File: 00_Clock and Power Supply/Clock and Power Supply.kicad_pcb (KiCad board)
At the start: 2 copper layers, 100 x 100 mm, 38 parts, among them J1 Output 1, J2 Output 2, J3 Jack-DC, Q1 TIP126, SW1 SPST, SW2 SPST, SW3 SW_SPDT, U1 L7805, U2 LM555xN, U3 LM555xN, U4 74LS01, U5 74LS01, U6 74LS01

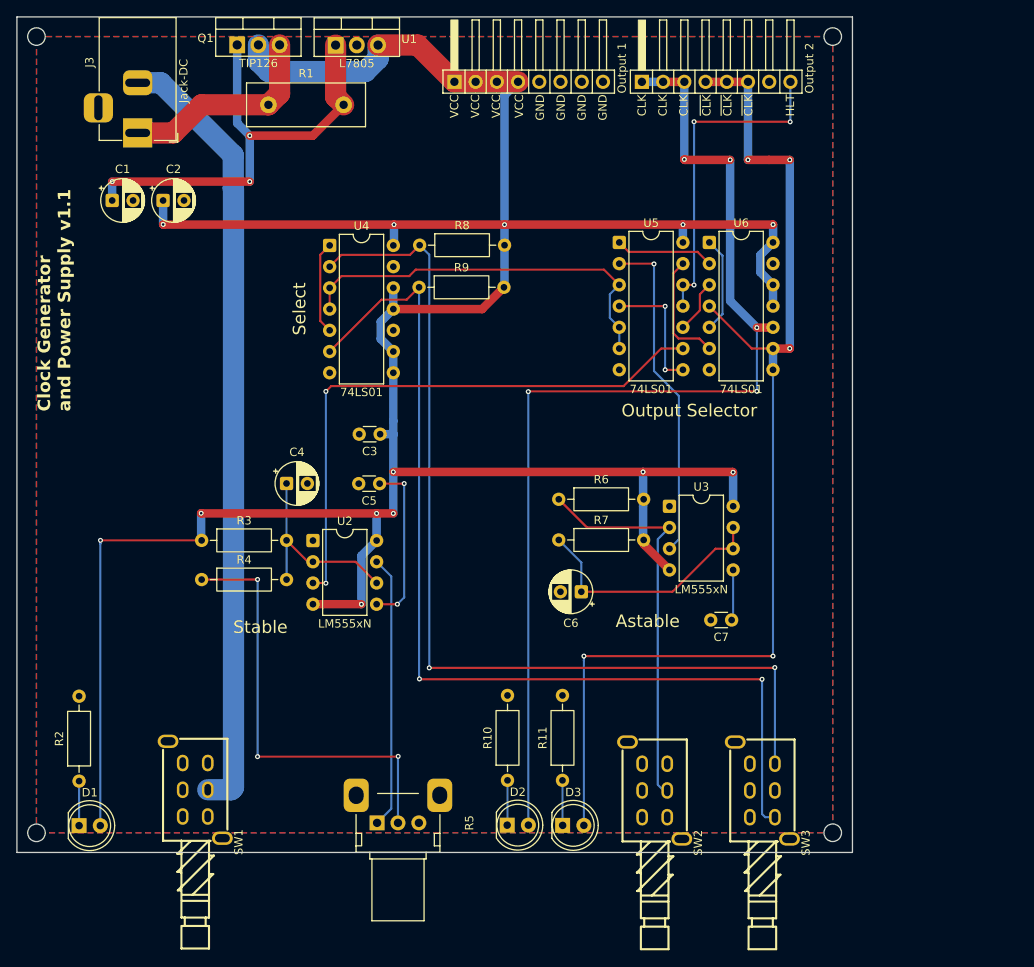
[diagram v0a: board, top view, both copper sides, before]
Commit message: Last revision of the cpu, all boards have been ordered. Implementation to be tested and documented in following commits.
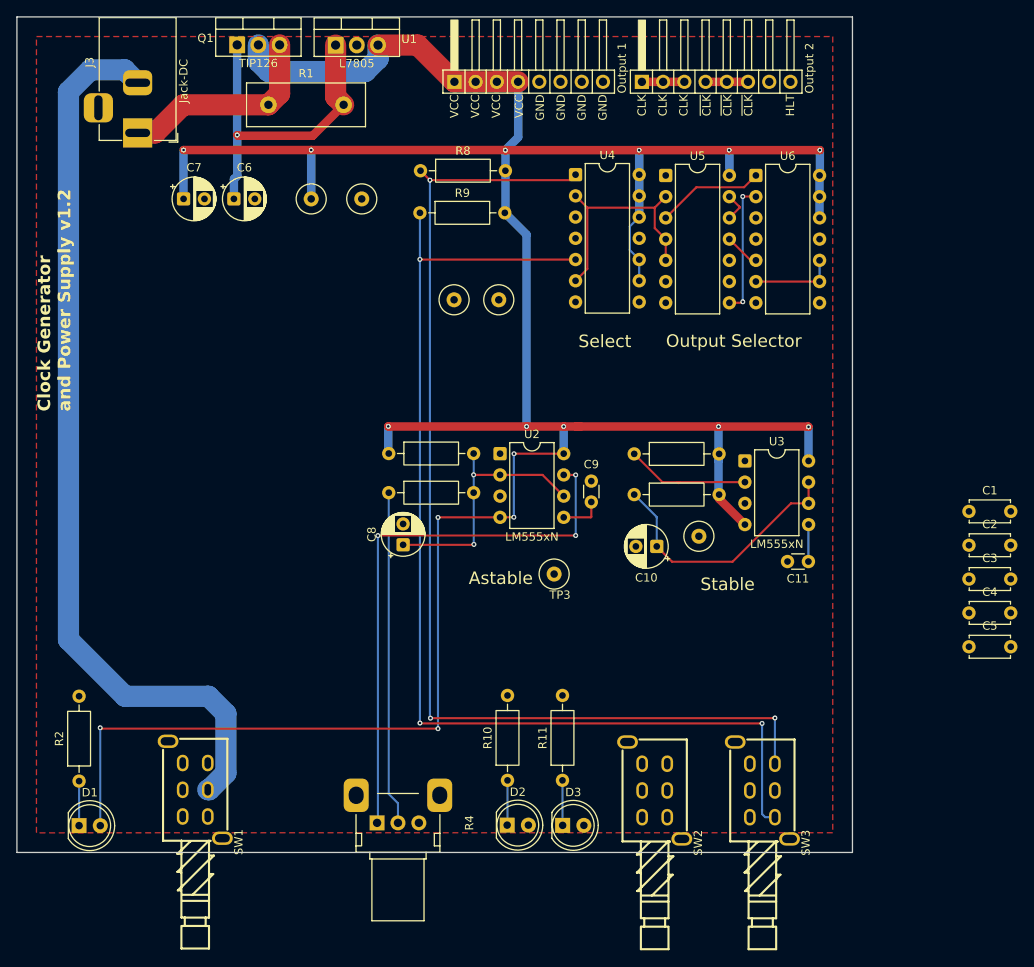
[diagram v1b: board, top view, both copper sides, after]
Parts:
- removed REF** (x4): MountingHole_2.1mm, MountingHole:MountingHole_2.1mm
- added C1: 100nF, Capacitor_THT:C_Disc_D4.7mm_W2.5mm_P5.00mm, F.Cu at (143.9, 89.2)
- added C2: 100nF, Capacitor_THT:C_Disc_D4.7mm_W2.5mm_P5.00mm, F.Cu at (143.9, 93.2)
- added C4: 100nF, Capacitor_THT:C_Disc_D4.7mm_W2.5mm_P5.00mm, F.Cu at (143.9, 101.3)
- added C5: 100nF, Capacitor_THT:C_Disc_D4.7mm_W2.5mm_P5.00mm, F.Cu at (143.9, 105.4)
- added TP1: VCC, TestPoint:TestPoint_Loop_D3.50mm_Drill0.9mm_Beaded, F.Cu at (65.2, 51.8)
- added TP2: GND, TestPoint:TestPoint_Loop_D3.50mm_Drill0.9mm_Beaded, F.Cu at (71.2, 51.8)
- added TP3: Astable, TestPoint:TestPoint_Loop_D3.50mm_Drill0.9mm_Beaded, F.Cu at (94.2, 96.7)
- added TP4: Stable, TestPoint:TestPoint_Loop_D3.50mm_Drill0.9mm_Beaded, F.Cu at (111.5, 92.2)
- added TP5: Select, TestPoint:TestPoint_Loop_D3.50mm_Drill0.9mm_Beaded, F.Cu at (82.2, 63.9)
- added TP6: HLT, TestPoint:TestPoint_Loop_D3.50mm_Drill0.9mm_Beaded, F.Cu at (87.6, 63.9)
- C3: value 100n -> 100nF; footprint Capacitor_THT:C_Disc_D3.0mm_W1.6mm_P2.50mm -> Capacitor_THT:C_Disc_D4.7mm_W2.5mm_P5.00mm
- U4, U5, U6: value 74LS01 -> 74LS00
- moved C3 72.6 mm to (143.9, 97.3), turned to 0 degrees
- moved U4 30.6 mm to (96.8, 48.9)
- moved C9 25.4 mm to (98.7, 88.1), turned to 90 degrees
- moved R3 24.7 mm to (74.4, 82.3)
- moved R5 24.7 mm to (74.4, 87.0)
- moved U2 24.7 mm to (87.8, 82.3)
- moved C8 15.8 mm to (76.2, 93.2), turned to 90 degrees
- moved C6 14.6 mm to (55.9, 51.8)
- moved C11 11.5 mm to (124.7, 95.2)
- moved R6 10.5 mm to (103.8, 82.3)
- moved R7 10.5 mm to (103.8, 87.2)
- moved U3 10.5 mm to (117.1, 83.2)
- moved C10 10.5 mm to (106.5, 93.4)
- moved U6 9.76 mm to (118.4, 49.0)
- moved U5 9.76 mm to (107.6, 49.0)
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- renumbered C6 to C10, C7 to C11, C1 to C6, C2 to C7, C4 to C8, C5 to C9, R5 to R4, R4 to R5
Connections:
- C3 pad 1: /VCC -> VCC
- C7 pad 1: /VCC -> VCC
- D1 pad 2: /VCC -> VCC
- D2 pad 2: /CLK -> CLK
- D3 pad 2: /~{CLK} -> ~{CLK}
- J1 pad 1: /VCC -> VCC
- J1 pad 2: /VCC -> VCC
- J1 pad 3: /VCC -> VCC
- J1 pad 4: /VCC -> VCC
- J2 pad 1: /CLK -> CLK
- J2 pad 2: /CLK -> CLK
- J2 pad 3: /CLK -> CLK
- J2 pad 4: /~{CLK} -> ~{CLK}
- J2 pad 5: /~{CLK} -> ~{CLK}
- J2 pad 6: /~{CLK} -> ~{CLK}
- J2 pad 8: /HLT -> HLT
- Q1 pad 2: /VCC -> VCC
- R3 pad 1: /VCC -> Net-(U2-DIS)
- R3 pad 2: Net-(U2-THR) -> VCC
- R4 pad 2: Net-(R4-Pad1) -> Net-(R4-Pad2)
- R5 pad 1: Net-(R4-Pad1) -> Net-(U2-THR)
- R5 pad 2: Net-(U2-THR) -> Net-(R4-Pad2)
- R6 pad 2: /VCC -> VCC
- R7 pad 2: /VCC -> VCC
- R8 pad 2: /VCC -> VCC
- R9 pad 2: /VCC -> VCC
- U1 pad 3: /VCC -> VCC
- U2 pad 4: /VCC -> VCC
- U2 pad 8: /VCC -> VCC
- U3 pad 4: /VCC -> VCC
- U3 pad 8: /VCC -> VCC
- U4 pad 1: Net-(U4-Pad1) -> Net-(SW3-A)
- U4 pad 10: unconnected-(U4-Pad10) -> VCC
- U4 pad 11: /VCC -> unconnected-(U4-Pad11)
- U4 pad 12: /VCC -> VCC
- U4 pad 13: unconnected-(U4-Pad13) -> VCC
- U4 pad 14: /VCC -> VCC
- U4 pad 2: Net-(SW3-A) -> /Clock Selector/Select
- U4 pad 3: /Clock Selector/Select -> Net-(U4-Pad3)
- U4 pad 4: /Clock Selector/Select -> Net-(U4-Pad3)
- U4 pad 5: Net-(U4-Pad1) -> Net-(SW3-C)
- U4 pad 6: Net-(SW3-C) -> /Clock Selector/Select
- U4 pad 8: /VCC -> unconnected-(U4-Pad8)
- U4 pad 9: /VCC -> VCC
- U5 pad 1: Net-(U5-Pad1) -> /Clock Selector/Stable
- U5 pad 10: Net-(U5-Pad10) -> /Astable Clock/Astable
- U5 pad 11: /HLT -> Net-(U5-Pad11)
- U5 pad 12: /HLT -> HLT
- U5 pad 13: Net-(U5-Pad13) -> HLT
- U5 pad 14: /VCC -> VCC
- U5 pad 2: /Clock Selector/Stable -> /Clock Selector/Select
- U5 pad 3: /Clock Selector/Select -> Net-(U5-Pad3)
- U5 pad 4: Net-(U5-Pad4) -> /Clock Selector/Select
- U5 pad 6: /Clock Selector/Select -> Net-(U5-Pad6)
- U5 pad 8: Net-(U5-Pad4) -> Net-(U5-Pad8)
- U5 pad 9: /Astable Clock/Astable -> Net-(U5-Pad6)
- U6 pad 1: Net-(U6-Pad1) -> Net-(U5-Pad3)
- U6 pad 10: /CLK -> ~{CLK}
- U6 pad 11: /VCC -> unconnected-(U6-Pad11)
- U6 pad 12: /VCC -> VCC
- U6 pad 13: unconnected-(U6-Pad13) -> VCC
- U6 pad 14: /VCC -> VCC
- U6 pad 2: Net-(U5-Pad1) -> Net-(U5-Pad8)
- U6 pad 3: Net-(U5-Pad10) -> Net-(U6-Pad3)
- U6 pad 4: /~{CLK} -> Net-(U6-Pad3)
- U6 pad 5: Net-(U6-Pad1) -> Net-(U5-Pad11)
- U6 pad 6: Net-(U5-Pad13) -> ~{CLK}
- U6 pad 8: /~{CLK} -> CLK
- U6 pad 9: /~{CLK} -> ~{CLK}
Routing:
- net VCC: track 0.00 -> 370.9 mm, vias 0 -> 16
- net /VCC: track 346.4 -> 0.00 mm, vias 13 -> 0
- net /~{CLK}: track 133.4 -> 0.00 mm, vias 5 -> 0
- net /CLK: track 130.3 -> 0.00 mm, vias 5 -> 0
- net /Astable Clock/Astable: track 69.4 -> 0.00 mm, vias 2 -> 0
- net Net-(R4-Pad1): track 52.7 -> 0.00 mm, vias 3 -> 0
- net Net-(U2-THR): track 24.4 -> 71.2 mm, vias 0 -> 2
- net /Clock Selector/Stable: track 40.0 -> 0.00 mm, vias 1 -> 0
- net /HLT: track 39.7 -> 0.00 mm, vias 3 -> 0
- net Net-(U2-DIS): track 32.7 -> 66.8 mm, vias 0 -> 3
- net Net-(U3-TR): track 47.5 -> 14.7 mm
- net /Clock Selector/Select: track 47.4 -> 28.1 mm
- net Net-(U5-Pad8): track 0.00 -> 15.8 mm, vias 0 -> 2
- net Net-(Q1-B): track 56.1 -> 40.4 mm, vias 3 -> 1
- net Net-(U5-Pad4): track 15.2 -> 0.00 mm, vias 2 -> 0
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- removed copper zone on B.Cu, net GND
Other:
- board text added: "Clock Generator and Power Supply v1.2"
- board text removed: "Clock Generator and Power Supply v1.1"
